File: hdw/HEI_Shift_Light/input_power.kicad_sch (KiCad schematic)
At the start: 17 parts

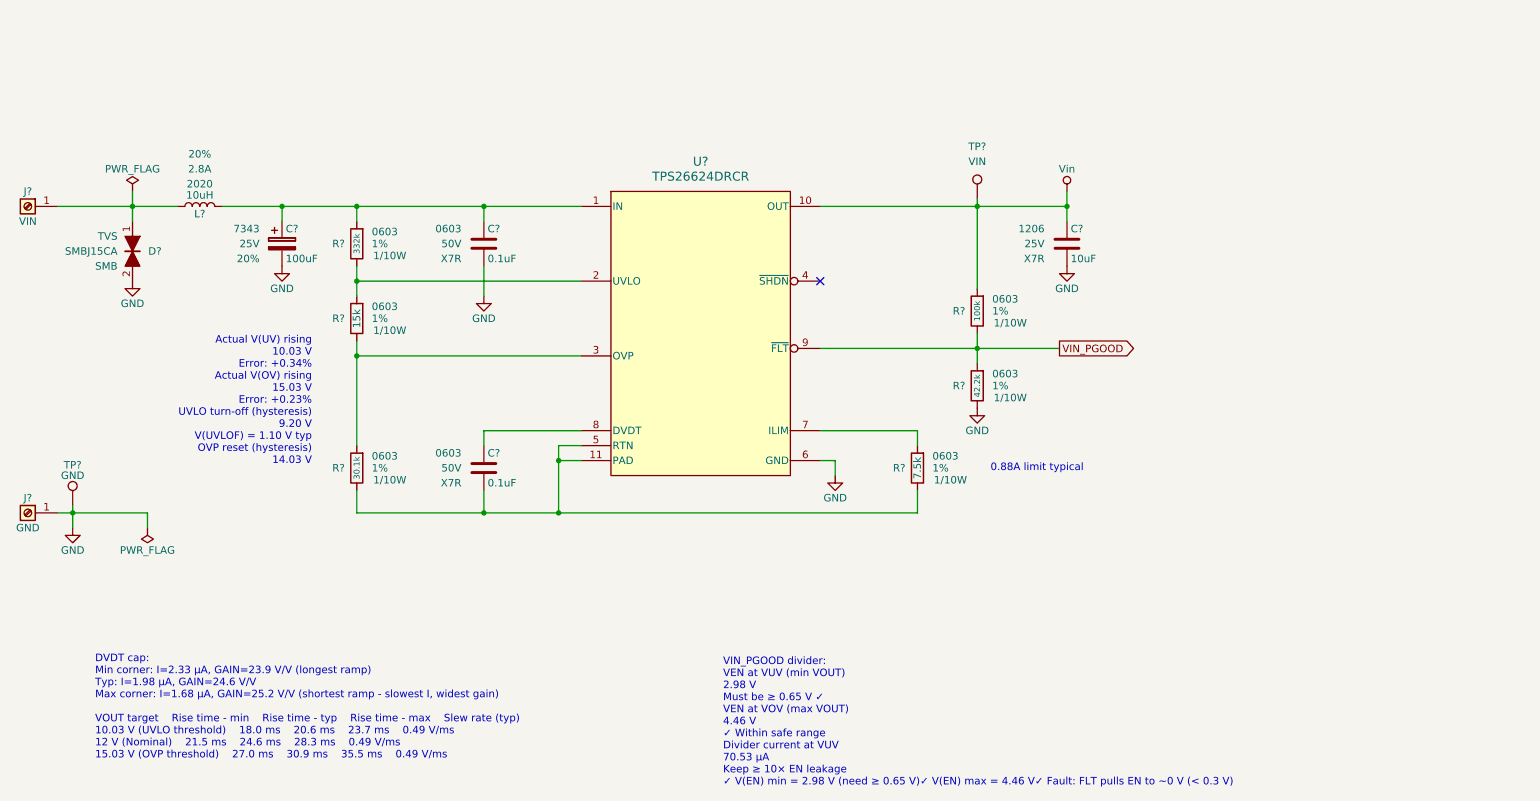
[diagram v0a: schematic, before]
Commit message: filled in digikey part numbers
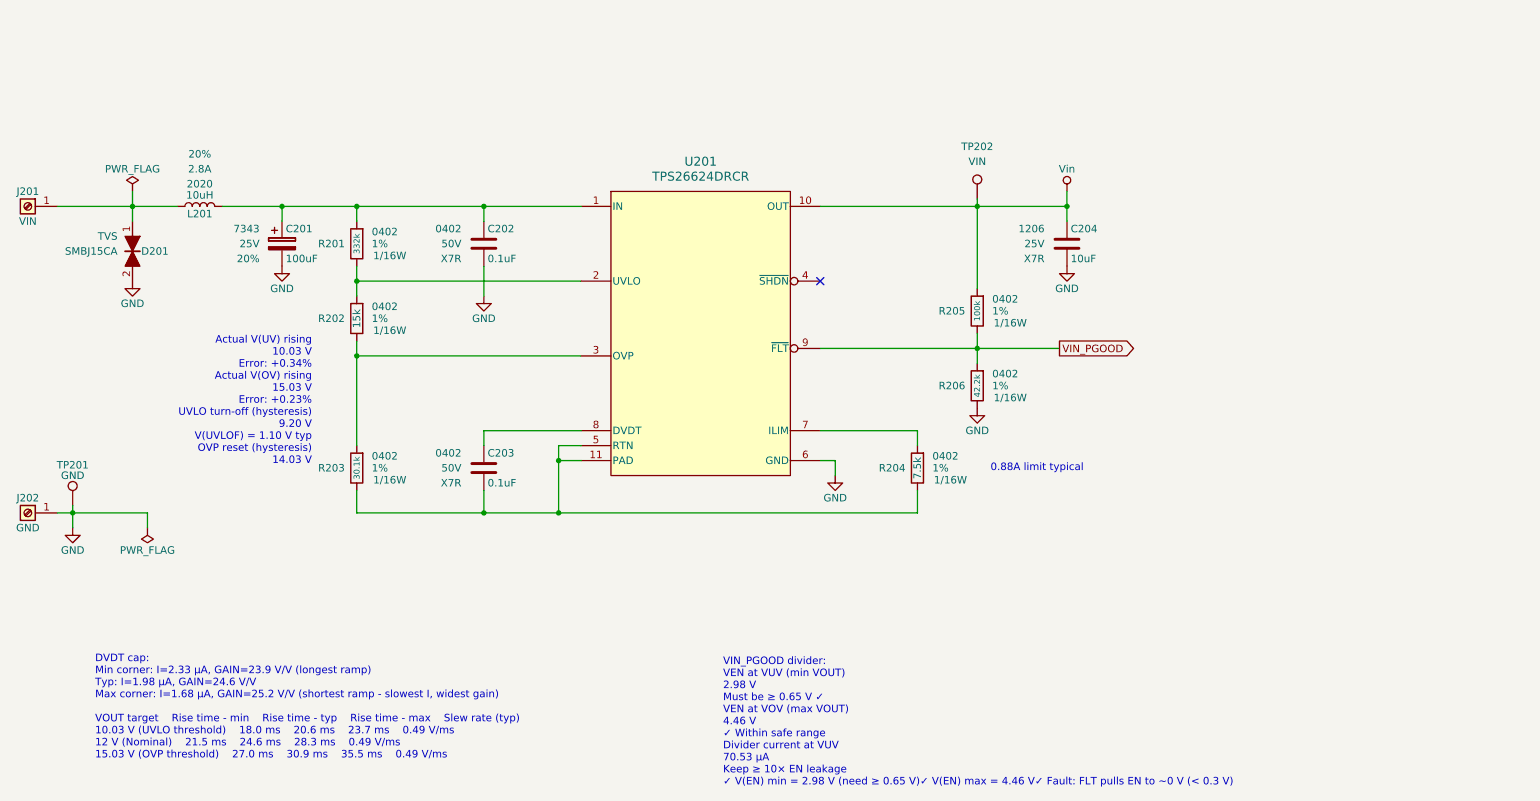
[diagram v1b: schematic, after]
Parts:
- C202, C203: renamed from C?; footprint Capacitors_SMD:C_0603 -> Capacitors_SMD:C_0402; display_footprint 0603 -> 0402
- D201: renamed from D?; Digi-Key PN (none) -> SMBJ15CA-E3-52GICT-ND; Footprint Display SMB -> (none); display_footprint (none) -> SMB
- J201, J202: renamed from J?; footprint (none) -> Keystone:7691; Digi-Key PN (none) -> 36-7691-ND; MPN (none) -> 7691; Manufacturer (none) -> Keystone Electronics
- R201: renamed from R?; footprint (none) -> Resistors_SMD:R_0402; Digi-Key PN (none) -> 541-332KLCT-ND; Wattage 1/10W -> 1/16W; display_footprint 0603 -> 0402
- R202: renamed from R?; footprint (none) -> Resistors_SMD:R_0402; Digi-Key PN (none) -> 541-15.0KLCT-ND; Wattage 1/10W -> 1/16W; display_footprint 0603 -> 0402
- R203: renamed from R?; footprint (none) -> Resistors_SMD:R_0402; Digi-Key PN (none) -> 541-4109-1-ND; Wattage 1/10W -> 1/16W; display_footprint 0603 -> 0402
- R204: renamed from R?; footprint (none) -> Resistors_SMD:R_0402; Digi-Key PN (none) -> 541-7.50KLCT-ND; Wattage 1/10W -> 1/16W; display_footprint 0603 -> 0402
- R205: renamed from R?; footprint (none) -> Resistors_SMD:R_0402; Digi-Key PN (none) -> 541-100KLCT-ND; Wattage 1/10W -> 1/16W; display_footprint 0603 -> 0402
- R206: renamed from R?; footprint (none) -> Resistors_SMD:R_0402; Digi-Key PN (none) -> 541-42.2KLCT-ND; Wattage 1/10W -> 1/16W; display_footprint 0603 -> 0402
- TP201: renamed from TP?; Digi-Key PN (none) -> SAM1051-01-ND
- U201: renamed from U?; Digi-Key PN (none) -> TPS26624DRCR-ND
- gave numbers to parts that had none: 4

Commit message: fixed some digikey pns
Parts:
- C202, C203: Digi-Key PN 399-7845-1-ND -> 1276-7069-1-ND
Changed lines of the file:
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@@
 			)
 		)
-		(property "Digi-Key PN" "399-7845-1-ND"
+		(property "Digi-Key PN" "1276-7069-1-ND"
 			(at 130.175 64.77 0)
 			(hide yes)
@@
 			)
 		)
-		(property "Digi-Key PN" "399-7845-1-ND"
+		(property "Digi-Key PN" "1276-7069-1-ND"
 			(at 130.175 102.87 0)
 			(hide yes)

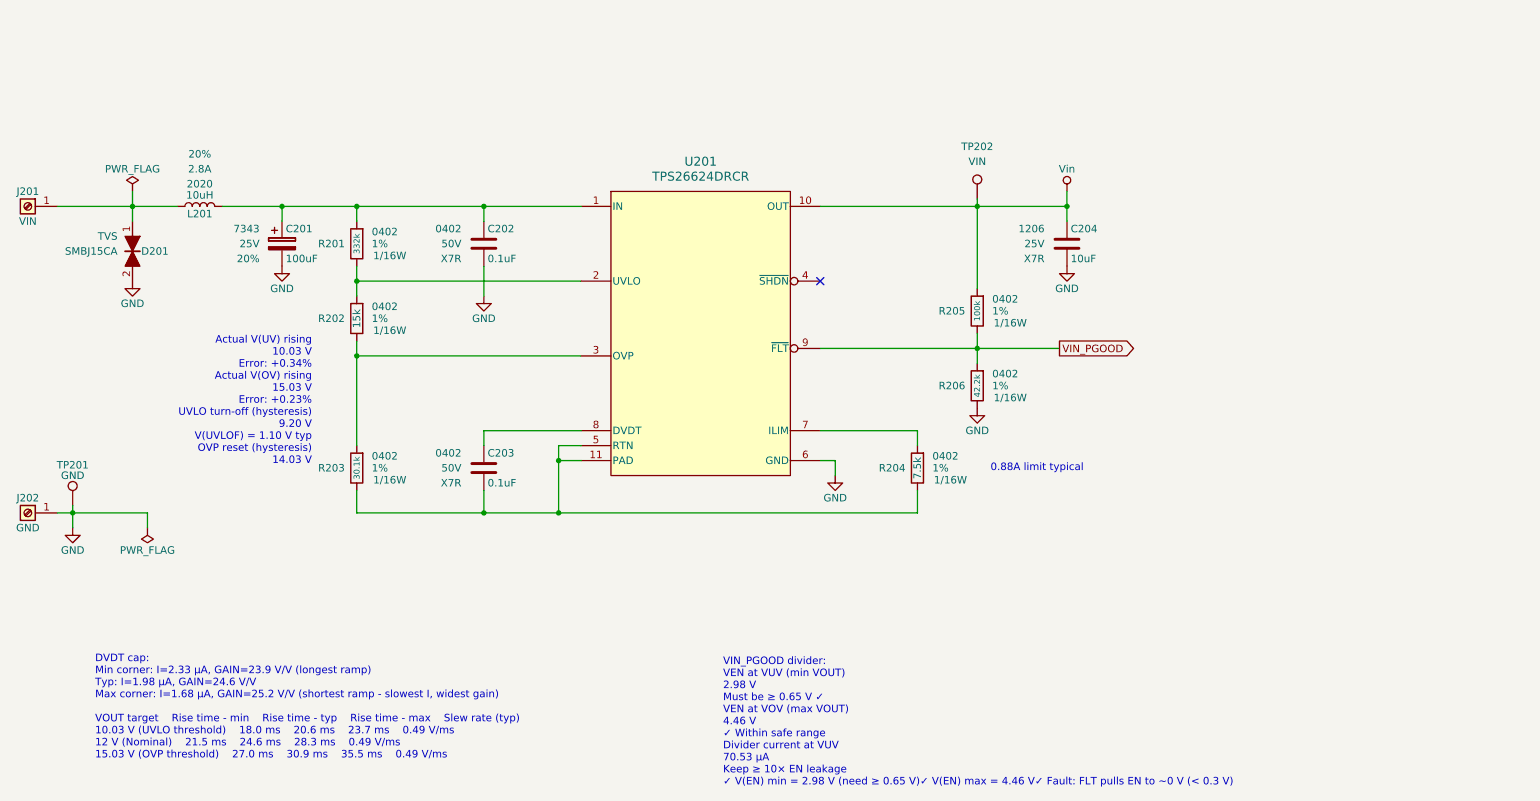
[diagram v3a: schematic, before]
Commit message: moved GND connections to mount holes, updated gitignore
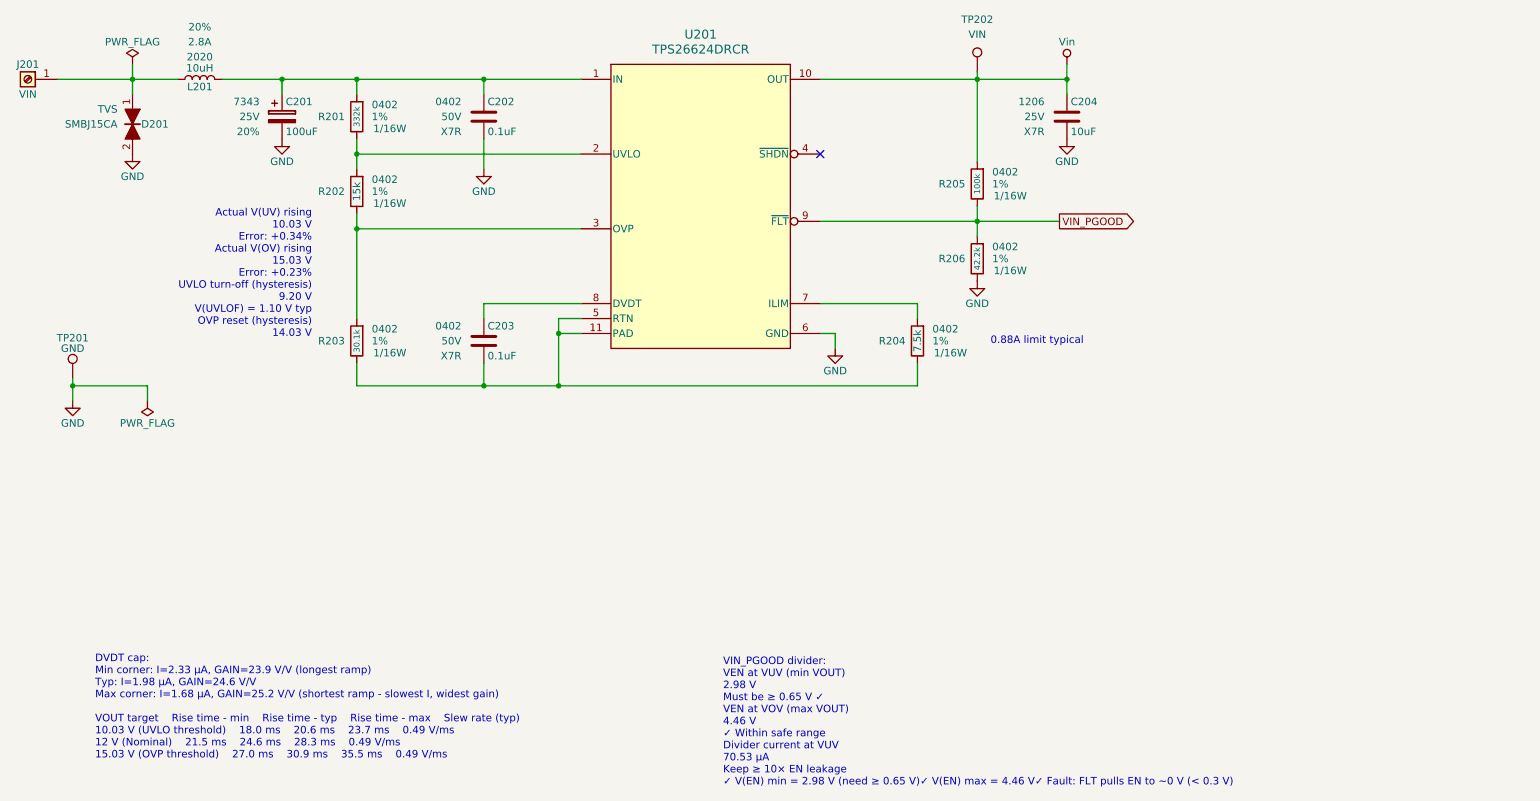
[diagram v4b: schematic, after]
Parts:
- removed J202: GND, Keystone:7691, symbol Connector:Screw_Terminal_01x01
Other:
- moved on the sheet: C201, C202, C203, C204, D201, J201, L201, R201, R202, R203, R204, R205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

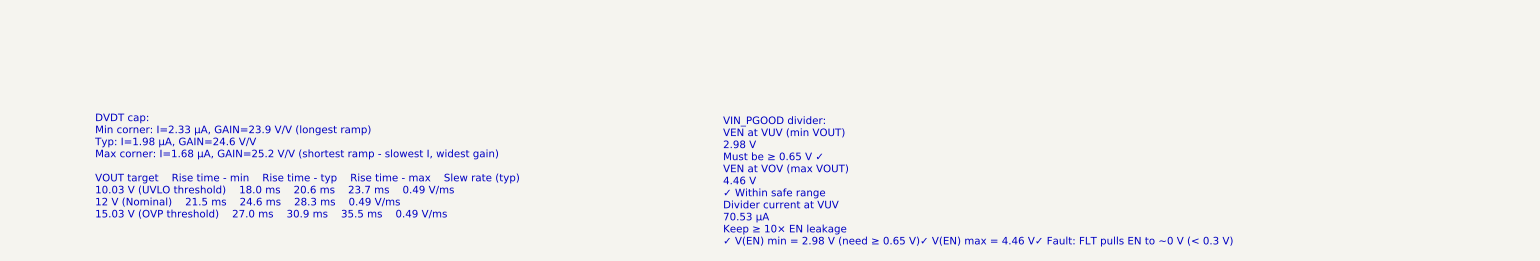
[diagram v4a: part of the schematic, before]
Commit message: added component datasheet properties
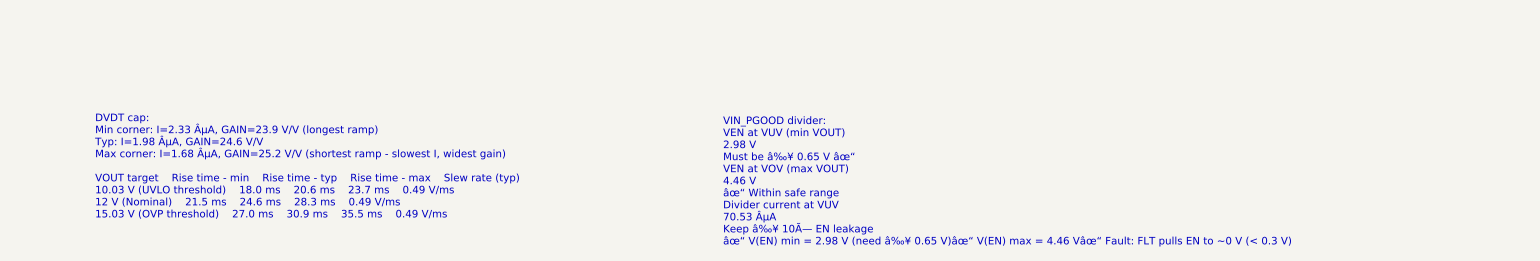
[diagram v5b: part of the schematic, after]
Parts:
- C202, C203: Digi-Key PN 1276-7069-1-ND -> 445-5932-1-ND
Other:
- note added: "DVDT cap: Min corner: I=2.33 ÂµA, GAIN=23.9 V/V (longest ramp) Typ: I=1.98 ÂµA, GAIN=24.6 V/V Max corner: I=1.68 ÂµA, GAIN=25.2 V/V (shortest ramp - slowest I, widest gain) VOUT target Rise time - min Rise time - typ Rise time - max Slew rate (typ) 10.03 V (UVLO threshold) 18.0 ms 20.6 ms 23.7 ms 0.49 V/ms 12 V (Nominal) 21.5 ms 24.6 ms 28.3 ms 0.49 V/ms 15.03 V (OVP threshold) 27.0 ms 30.9 ms 35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"
- note added: "VIN_PGOOD divider: VEN at VUV (min VOUT) 2.98 V Must be â‰¥ 0.65 V âœ“ VEN at VOV (max VOUT) 4.46 V âœ“ Within safe range Divider current at VUV 70.53 ÂµA Keep â‰¥ 10Ã— EN leakage âœ“ V(EN) min = 2.98 V (need â‰¥ 0.65 V)âœ“ V(EN) max = 4.46 Vâœ“ Fault: FLT pulls EN to ~0 V (< 0.3 V)"
- note removed: "DVDT cap: Min corner: I=2.33 µA, GAIN=23.9 V/V (longest ramp) Typ: I=1.98 µA, GAIN=24.6 V/V Max corner: I=1.68 µA, GAIN=25.2 V/V (shortest ramp - slowest I, widest gain) VOUT target Rise time - min Rise time - typ Rise time - max Slew rate (typ) 10.03 V (UVLO threshold) 18.0 ms 20.6 ms 23.7 ms 0.49 V/ms 12 V (Nominal) 21.5 ms 24.6 ms 28.3 ms 0.49 V/ms 15.03 V (OVP threshold) 27.0 ms 30.9 ms 35.5 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"
- note removed: "VIN_PGOOD divider: VEN at VUV (min VOUT) 2.98 V Must be ≥ 0.65 V ✓ VEN at VOV (max VOUT) 4.46 V ✓ Within safe range Divider current at VUV 70.53 µA Keep ≥ 10× EN leakage ✓ V(EN) min = 2.98 V (need ≥ 0.65 V)✓ V(EN) max = 4.46 V✓ Fault: FLT pulls EN to ~0 V (< 0.3 V)"
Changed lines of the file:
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@@
 		)
 	)
-	(text "VIN_PGOOD divider:\nVEN at VUV (min VOUT)\n2.98 V\nMust be ≥ 0.65 V ✓\nVEN at VOV (max VOUT)\n4.46 V\n✓ Within safe range\nDivider current at VUV\n70.53 µA\nKeep ≥ 10× EN leakage\n✓ V(EN) min = 2.98 V (need ≥ 0.65 V)✓ V(EN) max = 4.46 V✓ Fault: FLT pulls EN to ~0 V (< 0.3 V)"
+	(text "VIN_PGOOD divider:\nVEN at VUV (min VOUT)\n2.98 V\nMust be â‰¥ 0.65 V âœ“\nVEN at VOV (max VOUT)\n4.46 V\nâœ“ Within safe range\nDivider current at VUV\n70.53 ÂµA\nKeep â‰¥ 10Ã— EN leakage\nâœ“ V(EN) min = 2.98 V (need â‰¥ 0.65 V)âœ“ V(EN) max = 4.46 Vâœ“ Fault: FLT pulls EN to ~0 V (< 0.3 V)"
 		(exclude_from_sim no)
 		(at 160.02 158.75 0)
@@
 		)
 	)
-	(text "DVDT cap:\nMin corner: I=2.33 µA, GAIN=23.9 V/V (longest ramp)\nTyp: I=1.98 µA, GAIN=24.6 V/V\nMax corner: I=1.68 µA, GAIN=25.2 V/V (shortest ramp - slowest I, widest gain)\n\nVOUT target	Rise time - min	Rise time - typ	Rise time - max	Slew rate (typ)\n10.03 V (UVLO threshold)	18.0 ms	20.6 ms	23.7 ms	0.49 V/ms\n12 V (Nominal)	21.5 ms	24.6 ms	28.3 ms	0.49 V/ms\n15.03 V (OVP threshold)	27.0 ms	30.9 ms	35.5 ms	0.49 V/ms"
+	(text "DVDT cap:\nMin corner: I=2.33 ÂµA, GAIN=23.9 V/V (longest ramp)\nTyp: I=1.98 ÂµA, GAIN=24.6 V/V\nMax corner: I=1.68 ÂµA, GAIN=25.2 V/V (shortest ramp - slowest I, widest gain)\n\nVOUT target	Rise time - min	Rise time - typ	Rise time - max	Slew rate (typ)\n10.03 V (UVLO threshold)	18.0 ms	20.6 ms	23.7 ms	0.49 V/ms\n12 V (Nominal)	21.5 ms	24.6 ms	28.3 ms	0.49 V/ms\n15.03 V (OVP threshold)	27.0 ms	30.9 ms	35.5 ms	0.49 V/ms"
 		(exclude_from_sim no)
 		(at 53.34 156.21 0)
@@
 			)
 		)
-		(property "Datasheet" ""
+		(property "Datasheet" "https://www.vishay.com/docs/34563/ihlp-2020cz-8a.pdf"
 			(at 71.12 49.53 0)
 			(hide yes)
@@
 			)
 		)
-		(property "Datasheet" ""
+		(property "Datasheet" "https://www.vishay.com/docs/20035/dcrcwe3.pdf"
 			(at 97.79 93.98 0)
 			(hide yes)
@@
 			)
 		)
-		(property "Datasheet" ""
+		(property "Datasheet" "https://www.vishay.com/docs/88392/smbj.pdf"
 			(at 63.5 57.15 0)
+			(hide yes)
 			(show_name no)
 			(do_not_autoplace no)
@@
 			)
 		)
-		(property "Datasheet" ""
+		(property "Datasheet" "https://www.vishay.com/docs/20035/dcrcwe3.pdf"
 			(at 97.79 68.58 0)
 			(hide yes)
@@
 			)
 		)
-		(property "Datasheet" ""
+		(property "Datasheet" "https://www.keyelco.com/userAssets/file/K75p73.pdf"
 			(at 41.91 49.53 0)
 			(hide yes)
@@
 			)
 		)
-		(property "Datasheet" ""
+		(property "Datasheet" "https://www.vishay.com/docs/20035/dcrcwe3.pdf"
 			(at 203.2 67.31 0)
 			(hide yes)
@@
 			)
 		)
-		(property "Datasheet" ""
+		(property "Datasheet" "https://product.tdk.com/en/system/files/dam/doc/product/capacitor/ceramic/mlcc/charasheet/c1005x7r1h104k050bb.pdf"
 			(at 120.015 53.34 0)
 			(hide yes)
@@
 			)
 		)
-		(property "Digi-Key PN" "1276-7069-1-ND"
+		(property "Digi-Key PN" "445-5932-1-ND"
 			(at 130.175 43.18 0)
 			(hide yes)
@@
 			)
 		)
-		(property "Datasheet" ""
+		(property "Datasheet" "https://www.vishay.com/docs/20035/dcrcwe3.pdf"
 			(at 203.2 80.01 0)
 			(hide yes)
@@
 			)
 		)
-		(property "Datasheet" ""
+		(property "Datasheet" "https://mm.digikey.com/Volume0/opasdata/d220001/medias/docus/2322/CL31B106KAHZW6E_Spec.pdf"
 			(at 219.075 53.34 0)
 			(hide yes)
@@
 			)
 		)
-		(property "Datasheet" ""
+		(property "Datasheet" "https://yageogroup.com/content/datasheet/asset/file/KEM_T2076_T52X-530"
 			(at 85.725 53.34 0)
 			(hide yes)
@@
 			)
 		)
-		(property "Datasheet" ""
+		(property "Datasheet" "https://suddendocs.samtec.com/catalog_english/htsw_th.pdf"
 			(at 54.61 100.33 0)
 			(hide yes)
@@
 			)
 		)
-		(property "Datasheet" ""
+		(property "Datasheet" "https://www.vishay.com/docs/20035/dcrcwe3.pdf"
 			(at 97.79 55.88 0)
 			(hide yes)
@@
 			)
 		)
-		(property "Datasheet" ""
+		(property "Datasheet" "https://www.vishay.com/docs/20035/dcrcwe3.pdf"
 			(at 193.04 93.98 0)
 			(hide yes)
@@
 			)
 		)
-		(property "Datasheet" ""
+		(property "Datasheet" "https://product.tdk.com/en/system/files/dam/doc/product/capacitor/ceramic/mlcc/charasheet/c1005x7r1h104k050bb.pdf"
 			(at 120.015 91.44 0)
 			(hide yes)
@@
 			)
 		)
-		(property "Digi-Key PN" "1276-7069-1-ND"
+		(property "Digi-Key PN" "445-5932-1-ND"
 			(at 130.175 81.28 0)
 			(hide yes)

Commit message: cleaned up digikey pns
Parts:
- D201: Digi-Key PN SMBJ15CA-E3-52GICT-ND -> SMBJ15CA
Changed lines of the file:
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@@
 		(property "Intersheetrefs" "${INTERSHEET_REFS}"
 			(at 230.6177 73.66 0)
-			(hide yes)
 			(show_name no)
 			(do_not_autoplace no)
@@
 			)
 		)
-		(property "Digi-Key PN" "SMBJ15CA-E3-52GICT-ND"
+		(property "Digi-Key PN" "SMBJ15CA"
 			(at 59.69 57.15 0)
 			(hide yes)

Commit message: fixed some footprints, pulled into PCB
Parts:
- J201: footprint Keystone:7691 -> Custom Footprints Library:CONN_7691_KEY
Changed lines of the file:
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@@
 			)
 		)
-		(property "Footprint" "Keystone:7691"
+		(property "Footprint" "Custom Footprints Library:CONN_7691_KEY"
 			(at 41.91 49.53 0)
 			(hide yes)
